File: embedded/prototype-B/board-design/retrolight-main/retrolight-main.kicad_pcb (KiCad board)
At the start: 2 copper layers, 45 x 20.5 mm, 32 parts, among them J1 Conn_02x05_Odd_Even, U1 TLC59108xPW

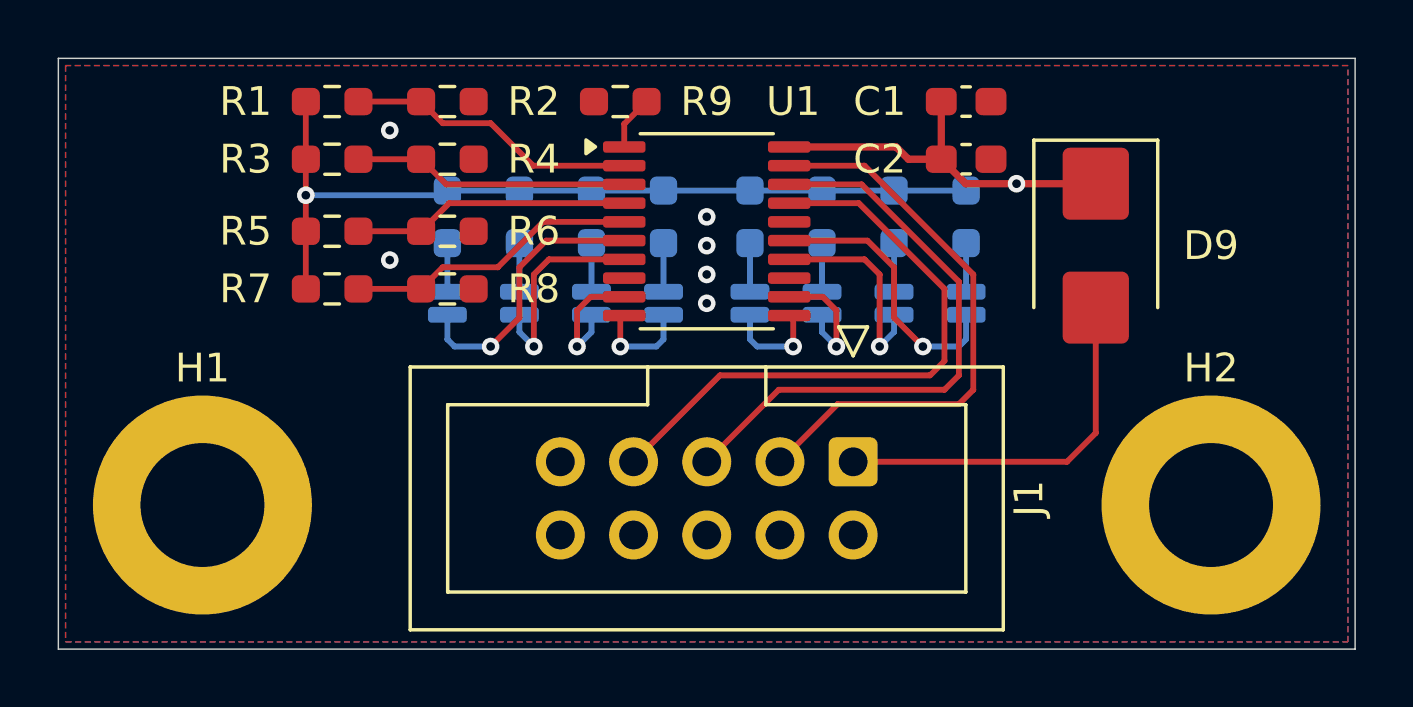
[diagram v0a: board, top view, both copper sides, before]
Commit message: [Light] Led driver reset pin enhacement
Refactored lighting PCB.

Signed-off-by: Nicolae-Andrei Prodan <vasilenicolaeandrei@gmail.com>
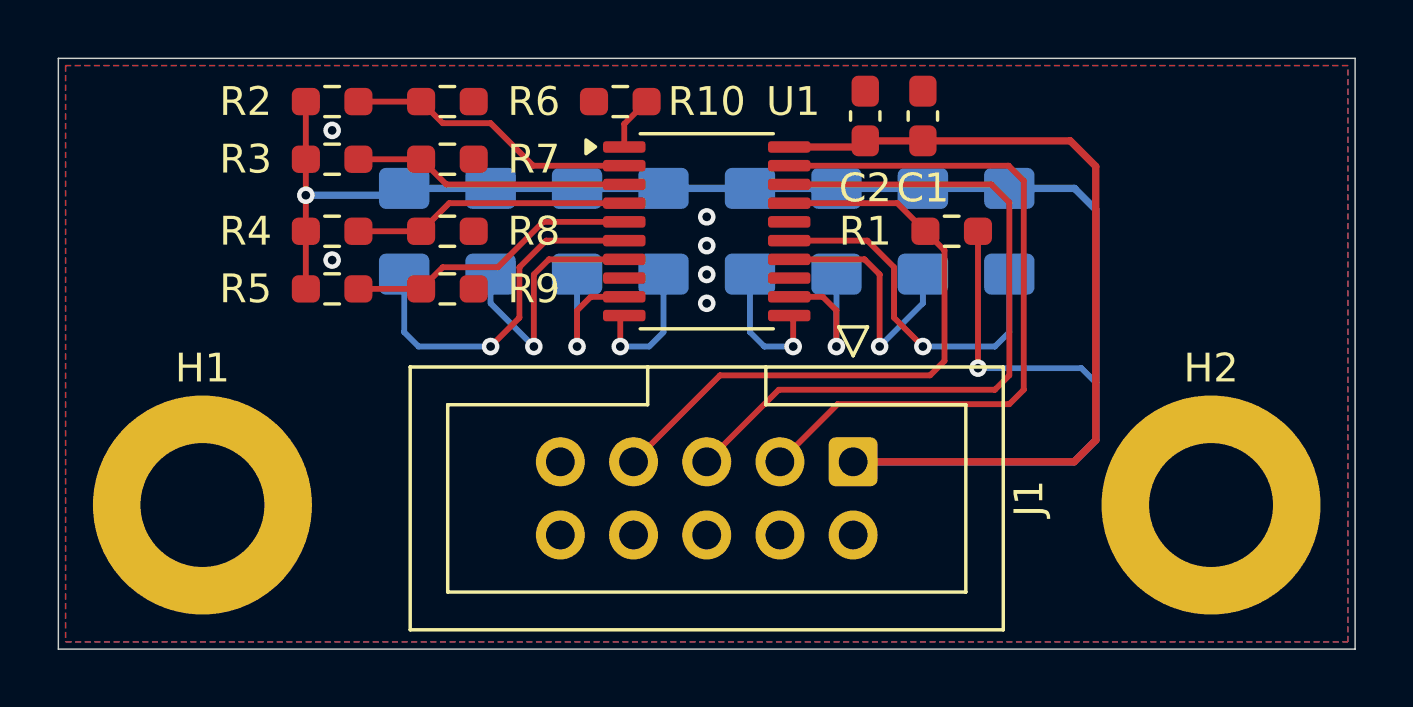
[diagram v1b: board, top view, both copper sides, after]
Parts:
- removed D9: MBRS130LT3G, Diode_SMD:D_SMB
- removed the R10 at (133.5, 90.0)
- removed R11, R12, R13, R14, R15, R16, R17: 0R/R0603, Resistor_SMD:R_0603_1608Metric_Pad0.98x0.95mm_HandSolder
- added R1: 10K/R0603, Resistor_SMD:R_0603_1608Metric_Pad0.98x0.95mm_HandSolder, F.Cu at (151.0, 90.5)
- D1, D2, D3, D4, D5, D6, D7, D8: value LED -> MP-3014-1100-50-70; footprint LED:LED_0505_1313Metric -> LED_SMD:LED_1206_3216Metric_Pad1.42x1.75mm_HandSolder
- R2: renamed from R1; value 10K/R0603(NC) -> 10K/R0603
- R3: value 10K/R0603(NC) -> 10K/R0603
- R4: renamed from R5; value 10K/R0603(NC) -> 10K/R0603
- R5: renamed from R7; value 10K/R0603(NC) -> 10K/R0603
- moved C2 3.81 mm to (148.0, 86.5), turned to 90 degrees
- moved D1 2.92 mm to (132.0, 90.5)
- moved D8 2.92 mm to (153.0, 90.5)
- moved D2 2.69 mm to (135.0, 90.5)
- moved D7 2.69 mm to (150.0, 90.5)
- moved D3 2.55 mm to (138.0, 90.5)
- moved D6 2.55 mm to (147.0, 90.5)
- moved D4 2.50 mm to (141.0, 90.5)
- moved D5 2.50 mm to (144.0, 90.5)
- moved C1 1.58 mm to (150.0, 86.5), turned to 90 degrees
- renumbered R9 to R10, R2 to R6, R4 to R7, R6 to R8, R8 to R9
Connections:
- D1 pad 2: Net-(D1-A) -> VCC
- D2 pad 2: Net-(D2-A) -> VCC
- D3 pad 2: Net-(D3-A) -> VCC
- D4 pad 2: Net-(D4-A) -> VCC
- D5 pad 2: Net-(D5-A) -> VCC
- D6 pad 2: Net-(D6-A) -> VCC
- D7 pad 2: Net-(D7-A) -> VCC
- D8 pad 2: Net-(D8-A) -> VCC
- J1 pad 1: Net-(D9-A) -> VCC
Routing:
- net VCC: track 44.5 -> 89.4 mm
- net Net-(D9-A): track 13.2 -> 0.00 mm
- net /SDA: track 19.7 -> 25.1 mm
- net /SCL: track 20.5 -> 25.6 mm
- net Net-(D8-K): track 9.64 -> 12.4 mm
- net Net-(D1-K): track 9.64 -> 12.4 mm
- net Net-(D7-K): track 7.16 -> 8.99 mm
- net Net-(D2-K): track 7.16 -> 8.99 mm
- net Net-(D8-A): track 1.69 -> 0.00 mm
- net Net-(D7-A): track 1.69 -> 0.00 mm
- net Net-(D6-A): track 1.69 -> 0.00 mm
- net Net-(D5-A): track 1.69 -> 0.00 mm
- net Net-(D4-A): track 1.69 -> 0.00 mm
- net Net-(D3-A): track 1.69 -> 0.00 mm
- net Net-(D2-A): track 1.69 -> 0.00 mm
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
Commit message: [Central unit] Redesign the power lines
Fixed lighting board footprint and resistor value issues. Redesigned
power path.

Signed-off-by: Nicolae-Andrei Prodan <vasilenicolaeandrei@gmail.com>
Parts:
- D1, D2, D3, D4, D5, D6, D7, D8: footprint LED_SMD:LED_1206_3216Metric_Pad1.42x1.75mm_HandSolder -> MP_3014_1100_50_70:LED_MP-3014-1100-50-70
- R10: value 375R/R0603 -> 750R/R0603
- turned D1 to -90 degrees
- turned D2 to -90 degrees
- turned D3 to -90 degrees
- turned D4 to -90 degrees
- turned D5 to -90 degrees
- turned D6 to -90 degrees
- turned D7 to -90 degrees
- turned D8 to -90 degrees
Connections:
- U1 pad 10: Net-(D4-K) -> Net-(U1-~{OUT3})
- U1 pad 11: Net-(D5-K) -> Net-(U1-~{OUT4})
- U1 pad 12: Net-(D6-K) -> Net-(U1-~{OUT5})
- U1 pad 14: Net-(D7-K) -> Net-(U1-~{OUT6})
- U1 pad 15: Net-(D8-K) -> Net-(U1-~{OUT7})
- U1 pad 6: Net-(D1-K) -> Net-(U1-~{OUT0})
- U1 pad 7: Net-(D2-K) -> Net-(U1-~{OUT1})
- U1 pad 9: Net-(D3-K) -> Net-(U1-~{OUT2})
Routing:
- net VCC: track 89.4 -> 17.9 mm
- net Net-(U1-~{OUT7}): track 0.00 -> 13.1 mm, vias 0 -> 1
- net Net-(U1-~{OUT0}): track 0.00 -> 13.1 mm, vias 0 -> 1
- net Net-(D8-K): track 12.4 -> 0.00 mm, vias 1 -> 0
- net Net-(D1-K): track 12.4 -> 0.00 mm, vias 1 -> 0
- net Net-(U1-~{OUT6}): track 0.00 -> 9.65 mm, vias 0 -> 1
- net Net-(U1-~{OUT1}): track 0.00 -> 9.65 mm, vias 0 -> 1
- net Net-(D7-K): track 8.99 -> 0.00 mm, vias 1 -> 0
- net Net-(D2-K): track 8.99 -> 0.00 mm, vias 1 -> 0
- net Net-(U1-~{OUT5}): track 0.00 -> 6.26 mm, vias 0 -> 1
- net Net-(U1-~{OUT2}): track 0.00 -> 6.26 mm, vias 0 -> 1
- net Net-(D6-K): track 5.60 -> 0.00 mm, vias 1 -> 0
- net Net-(D3-K): track 5.60 -> 0.00 mm, vias 1 -> 0
- net Net-(U1-~{OUT4}): track 0.00 -> 5.51 mm, vias 0 -> 1
- net Net-(U1-~{OUT3}): track 0.00 -> 5.51 mm, vias 0 -> 1
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- added copper zone on B.Cu, net VCC
- added copper zone on F.Cu, net VCC

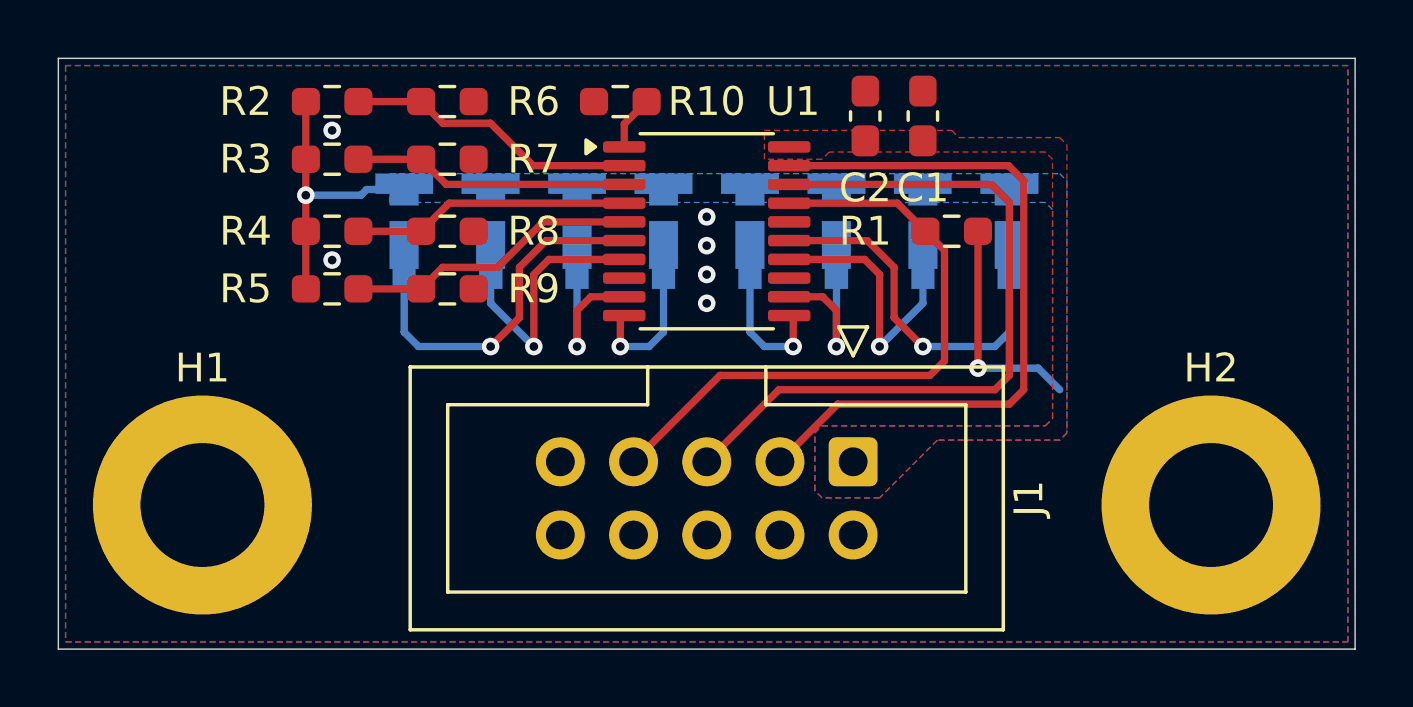
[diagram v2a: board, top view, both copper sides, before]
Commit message: [All] Enhance BOM
Enhanced lighting board BOM to include PCBWay required fields

Signed-off-by: Nicolae-Andrei Prodan <vasilenicolaeandrei@gmail.com>
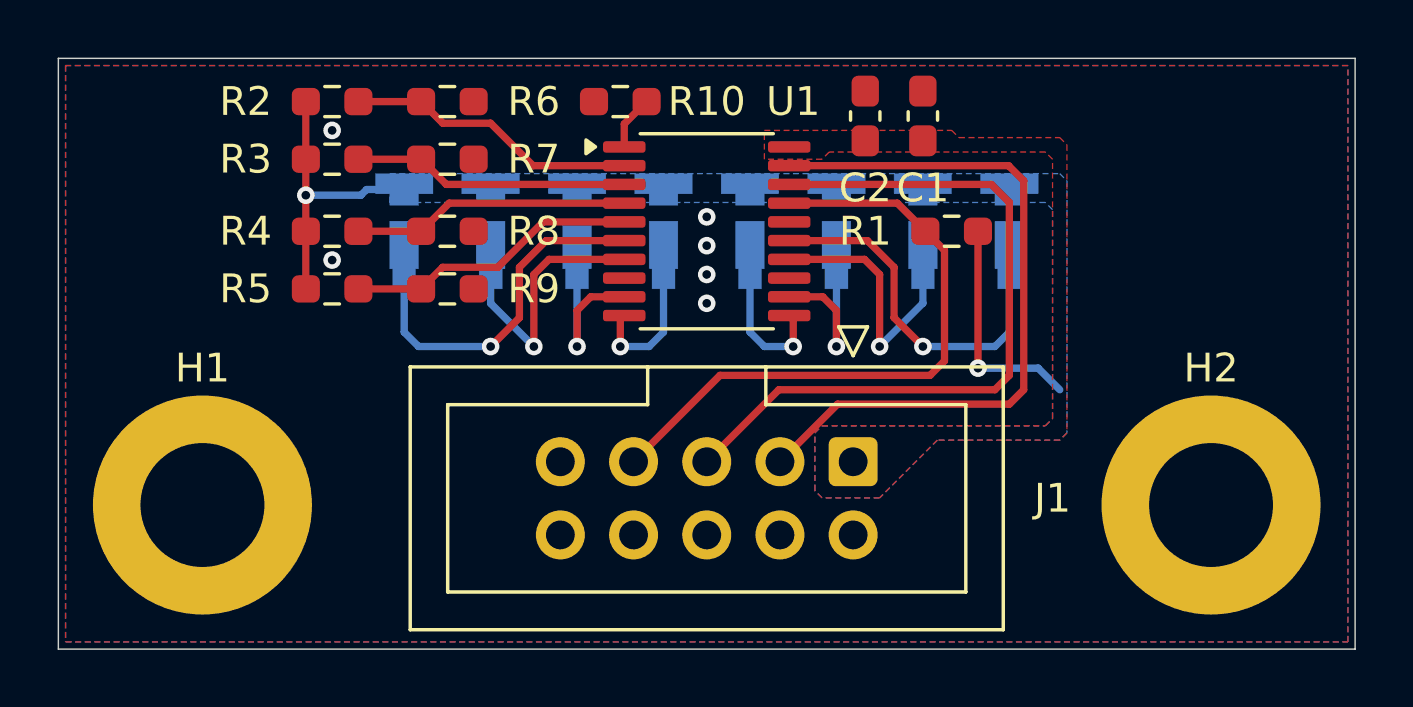
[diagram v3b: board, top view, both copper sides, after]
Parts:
- C1: value 10uF/6.3V/20%/C0603 -> 10uF/16V/10%C0603
- C2: value 100nF/6.3V/20%/C0603 -> 100nF/16V/10%C0603
- R1, R2, R3, R4, R5: value 10K/R0603 -> 10K/0.1W/1%/R0603
- R10: value 750R/R0603 -> 750R/0.1W/1%/R0603
- R6, R7, R8, R9: value 0R/R0603 -> 0R/0.1W/JUMPER/R0603
